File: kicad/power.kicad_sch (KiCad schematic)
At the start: 102 parts

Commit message: Fixed symbol missmatches from upgrading to kicad 6
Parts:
- C? (x16): symbol Device:CP_Small -> Device:C_Polarized_Small
- NT? (x6): symbol Device:Net-Tie_2 -> Device:NetTie_2
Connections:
- net +12V: now also NT?.2
- net +5V: now also NT?.2
- net GND: now also C?.2, C?.2, C?.2, C?.2, C?.2, C?.2, C?.2, C?.2, C?.2, C?.2
- net SVOUT: now also NT?.2
- net VDD: now also C?.1, NT?.1, NT?.1, NT?.1
- net at C?.1, C?.1, U?.2 (VIN)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: now also C?.1, C?.1, NT?.2 (x3)
- net at C?.1, C?.1, C?.2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: now also C?.1, C?.1, NT?.1
- net at Q?.1 (B), R?.1, R?.2: now also C?.1
- net at C?.1, C?.1, C?.1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: now also C?.1, C?.1, NT?.1 (x2)
- new net: C?.2, C?.2 (x3)
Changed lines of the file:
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@@
     (pin "1")
   )
-  (symbol (lib_id "Device:CP_Small") (at 189.865 52.705 0) (unit 1)
+  (symbol (lib_id "Device:C_Polarized_Small") (at 189.865 52.705 0) (unit 1)
     (in_bom yes) (on_board yes)
     (property "Reference" "C?" (id 0) (at 192.1002 51.5366 0)
@@
       (effects (font (size 1.27 1.27)) hide)
     )
+    (pin "1")
+    (pin "2")
   )
   (symbol (lib_id "Diode_Bridge:GBU6M") (at 177.8 50.165 0) (unit 1)
@@
     (pin "4")
   )
-  (symbol (lib_id "power:PWR_FLAG") (at 30.48 25.4 270)
+  (symbol (lib_id "power:PWR_FLAG") (at 30.48 25.4 270) (unit 1)
     (in_bom yes) (on_board yes)
     (property "Reference" "#FLG?" (id 0) (at 32.385 25.4 0)
@@
     (pin "1")
   )
-  (symbol (lib_id "power:PWR_FLAG") (at 30.48 27.94 270)
+  (symbol (lib_id "power:PWR_FLAG") (at 30.48 27.94 270) (unit 1)
     (in_bom yes) (on_board yes)
     (property "Reference" "#FLG?" (id 0) (at 32.385 27.94 0)
@@
     (pin "1")
   )
-  (symbol (lib_id "Device:CP_Small") (at 200.025 52.705 0) (unit 1)
+  (symbol (lib_id "Device:C_Polarized_Small") (at 200.025 52.705 0) (unit 1)
     (in_bom yes) (on_board yes)
     (property "Reference" "C?" (id 0) (at 202.2602 51.5366 0)
@@
       (effects (font (size 1.27 1.27)) hide)
     )
+    (pin "1")
+    (pin "2")
   )
   (symbol (lib_id "power:GND") (at 189.865 55.245 0) (unit 1)
@@
     (pin "2")
   )
-  (symbol (lib_id "Device:CP_Small") (at 232.41 56.515 0) (unit 1)
+  (symbol (lib_id "Device:C_Polarized_Small") (at 232.41 56.515 0) (unit 1)
     (in_bom yes) (on_board yes)
     (property "Reference" "C?" (id 0) (at 226.695 55.88 0)
@@
       (effects (font (size 1.27 1.27)) hide)
     )
+    (pin "1")
+    (pin "2")
   )
   (symbol (lib_id "power:GND") (at 232.41 62.23 0) (unit 1)
@@
     (pin "2")
   )
-  (symbol (lib_id "Device:CP_Small") (at 109.22 117.475 0) (mirror y) (unit 1)
+  (symbol (lib_id "Device:C_Polarized_Small") (at 109.22 117.475 0) (mirror y) (unit 1)
     (in_bom yes) (on_board yes)
     (property "Reference" "C?" (id 0) (at 114.3 116.205 0)
@@
       (effects (font (size 1.27 1.27)) hide)
     )
-  )
-  (symbol (lib_id "Device:CP_Small") (at 109.22 109.22 180) (unit 1)
+    (pin "1")
+    (pin "2")
+  )
+  (symbol (lib_id "Device:C_Polarized_Small") (at 109.22 109.22 180) (unit 1)
     (in_bom yes) (on_board yes)
     (property "Reference" "C?" (id 0) (at 113.665 107.95 0)
@@
       (effects (font (size 1.27 1.27)) hide)
     )
+    (pin "1")
+    (pin "2")
   )
   (symbol (lib_id "Device:C_Small") (at 29.845 111.76 0) (unit 1)
@@
     (pin "2")
   )
-  (symbol (lib_id "Device:CP_Small") (at 29.845 104.14 180) (unit 1)
+  (symbol (lib_id "Device:C_Polarized_Small") (at 29.845 104.14 180) (unit 1)
     (in_bom yes) (on_board yes)
     (property "Reference" "C?" (id 0) (at 34.925 105.41 0)
@@
       (effects (font (size 1.27 1.27)) hide)
     )
-  )
-  (symbol (lib_id "Device:CP_Small") (at 21.59 104.14 180) (unit 1)
+    (pin "1")
+    (pin "2")
+  )
+  (symbol (lib_id "Device:C_Polarized_Small") (at 21.59 104.14 180) (unit 1)
     (in_bom yes) (on_board yes)
     (property "Reference" "C?" (id 0) (at 26.67 105.41 0)
@@
       (effects (font (size 1.27 1.27)) hide)
     )
-  )
-  (symbol (lib_id "power:VDD") (at 15.875 106.045 0)
+    (pin "1")
+    (pin "2")
+  )
+  (symbol (lib_id "power:VDD") (at 15.875 106.045 0) (unit 1)
     (in_bom yes) (on_board yes)
     (property "Reference" "#PWR?" (id 0) (at 15.875 109.855 0)
@@
     (pin "2")
   )
-  (symbol (lib_id "Device:CP_Small") (at 29.21 53.34 180) (unit 1)
+  (symbol (lib_id "Device:C_Polarized_Small") (at 29.21 53.34 180) (unit 1)
     (in_bom yes) (on_board yes)
     (property "Reference" "C?" (id 0) (at 34.29 54.61 0)
@@
       (effects (font (size 1.27 1.27)) hide)
     )
-  )
-  (symbol (lib_id "Device:CP_Small") (at 20.955 53.34 180) (unit 1)
+    (pin "1")
+    (pin "2")
+  )
+  (symbol (lib_id "Device:C_Polarized_Small") (at 20.955 53.34 180) (unit 1)
     (in_bom yes) (on_board yes)
     (property "Reference" "C?" (id 0) (at 26.035 54.61 0)
@@
       (effects (font (size 1.27 1.27)) hide)
     )
-  )
-  (symbol (lib_id "power:VDD") (at 15.24 55.245 0)
+    (pin "1")
+    (pin "2")
+  )
+  (symbol (lib_id "power:VDD") (at 15.24 55.245 0) (unit 1)
     (in_bom yes) (on_board yes)
     (property "Reference" "#PWR?" (id 0) (at 15.24 59.055 0)
@@
     (pin "1")
   )
-  (symbol (lib_id "Device:Net-Tie_2") (at 18.415 57.15 0) (unit 1)
+  (symbol (lib_id "Device:NetTie_2") (at 18.415 57.15 0) (unit 1)
     (in_bom yes) (on_board yes)
     (property "Reference" "NT?" (id 0) (at 18.415 55.88 0))
@@
       (effects (font (size 1.27 1.27)) hide)
     )
-  )
-  (symbol (lib_id "Device:Net-Tie_2") (at 19.05 107.95 0) (unit 1)
+    (pin "1")
+    (pin "2")
+  )
+  (symbol (lib_id "Device:NetTie_2") (at 19.05 107.95 0) (unit 1)
     (in_bom yes) (on_board yes)
     (property "Reference" "NT?" (id 0) (at 19.05 106.68 0))
@@
       (effects (font (size 1.27 1.27)) hide)
     )
+    (pin "1")
+    (pin "2")
   )
   (symbol (lib_id "power:GND") (at 78.105 147.32 0) (unit 1)
@@
     (pin "2")
   )
-  (symbol (lib_id "Device:CP_Small") (at 99.695 66.675 0) (mirror y) (unit 1)
+  (symbol (lib_id "Device:C_Polarized_Small") (at 99.695 66.675 0) (mirror y) (unit 1)
     (in_bom yes) (on_board yes)
     (property "Reference" "C?" (id 0) (at 104.775 65.405 0)
@@
       (effects (font (size 1.27 1.27)) hide)
     )
-  )
-  (symbol (lib_id "Device:CP_Small") (at 99.695 58.42 180) (unit 1)
+    (pin "1")
+    (pin "2")
+  )
+  (symbol (lib_id "Device:C_Polarized_Small") (at 99.695 58.42 180) (unit 1)
     (in_bom yes) (on_board yes)
     (property "Reference" "C?" (id 0) (at 104.14 57.15 0)
@@
       (effects (font (size 1.27 1.27)) hide)
     )
+    (pin "1")
+    (pin "2")
   )
   (symbol (lib_id "power:GND") (at 80.01 69.85 0) (unit 1)
@@
     (pin "2")
   )
-  (symbol (lib_id "Device:Net-Tie_2") (at 106.045 62.23 0) (unit 1)
+  (symbol (lib_id "Device:NetTie_2") (at 106.045 62.23 0) (unit 1)
     (in_bom yes) (on_board yes)
     (property "Reference" "NT?" (id 0) (at 106.045 60.96 0))
@@
       (effects (font (size 1.27 1.27)) hide)
     )
-  )
-  (symbol (lib_id "Device:Net-Tie_2") (at 115.57 113.03 0) (unit 1)
+    (pin "1")
+    (pin "2")
+  )
+  (symbol (lib_id "Device:NetTie_2") (at 115.57 113.03 0) (unit 1)
     (in_bom yes) (on_board yes)
     (property "Reference" "NT?" (id 0) (at 115.57 111.76 0))
@@
       (effects (font (size 1.27 1.27)) hide)
     )
+    (pin "1")
+    (pin "2")
   )
   (symbol (lib_id "Device:R") (at 78.105 142.24 0) (unit 1)
@@
     )
   )
-  (symbol (lib_id "Device:CP_Small") (at 242.57 44.45 0) (unit 1)
+  (symbol (lib_id "Device:C_Polarized_Small") (at 242.57 44.45 0) (unit 1)
     (in_bom yes) (on_board yes)
     (property "Reference" "C?" (id 0) (at 244.8052 43.2816 0)
@@
       (effects (font (size 1.27 1.27)) hide)
     )
+    (pin "1")
+    (pin "2")
   )
   (symbol (lib_id "power:GND") (at 242.57 46.99 0) (unit 1)
@@
     (pin "2")
   )
-  (symbol (lib_id "Device:CP_Small") (at 227.33 117.475 0) (mirror y) (unit 1)
+  (symbol (lib_id "Device:C_Polarized_Small") (at 227.33 117.475 0) (mirror y) (unit 1)
     (in_bom yes) (on_board yes)
     (property "Reference" "C?" (id 0) (at 232.41 116.205 0)
@@
       (effects (font (size 1.27 1.27)) hide)
     )
+    (pin "1")
+    (pin "2")
   )
   (symbol (lib_id "Device:C_Small") (at 147.955 111.76 0) (unit 1)
@@
     (pin "2")
   )
-  (symbol (lib_id "Device:CP_Small") (at 147.955 104.14 180) (unit 1)
+  (symbol (lib_id "Device:C_Polarized_Small") (at 147.955 104.14 180) (unit 1)
     (in_bom yes) (on_board yes)
     (property "Reference" "C?" (id 0) (at 153.035 105.41 0)
@@
       (effects (font (size 1.27 1.27)) hide)
     )
-  )
-  (symbol (lib_id "Device:CP_Small") (at 139.7 104.14 180) (unit 1)
+    (pin "1")
+    (pin "2")
+  )
+  (symbol (lib_id "Device:C_Polarized_Small") (at 139.7 104.14 180) (unit 1)
     (in_bom yes) (on_board yes)
     (property "Reference" "C?" (id 0) (at 144.78 105.41 0)
@@
       (effects (font (size 1.27 1.27)) hide)
     )
-  )
-  (symbol (lib_id "power:VDD") (at 133.985 106.045 0)
+    (pin "1")
+    (pin "2")
+  )
+  (symbol (lib_id "power:VDD") (at 133.985 106.045 0) (unit 1)
     (in_bom yes) (on_board yes)
     (property "Reference" "#PWR?" (id 0) (at 133.985 109.855 0)
@@
     (pin "1")
   )
-  (symbol (lib_id "Device:Net-Tie_2") (at 137.16 107.95 0) (unit 1)
+  (symbol (lib_id "Device:NetTie_2") (at 137.16 107.95 0) (unit 1)
     (in_bom yes) (on_board yes)
     (property "Reference" "NT?" (id 0) (at 137.16 106.68 0))
@@
       (effects (font (size 1.27 1.27)) hide)
     )
+    (pin "1")
+    (pin "2")
   )
   (symbol (lib_id "Device:R") (at 196.215 132.715 0) (unit 1)
@@
     (pin "2")
   )
-  (symbol (lib_id "Device:CP_Small") (at 227.33 109.22 180) (unit 1)
+  (symbol (lib_id "Device:C_Polarized_Small") (at 227.33 109.22 180) (unit 1)
     (in_bom yes) (on_board yes)
     (property "Reference" "C?" (id 0) (at 231.775 107.95 0)
@@
       (effects (font (size 1.27 1.27)) hide)
     )
-  )
-  (symbol (lib_id "Device:Net-Tie_2") (at 233.68 113.03 0) (unit 1)
+    (pin "1")
+    (pin "2")
+  )
+  (symbol (lib_id "Device:NetTie_2") (at 233.68 113.03 0) (unit 1)
     (in_bom yes) (on_board yes)
     (property "Reference" "NT?" (id 0) (at 233.68 111.76 0))
@@
       (effects (font (size 1.27 1.27)) hide)
     )
+    (pin "1")
+    (pin "2")
   )
   (symbol (lib_id "power:+5V") (at 243.84 111.125 0) (unit 1)

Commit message: Fixed broken connections
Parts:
- removed NT? (x6): Net-Tie_2, symbol Device:NetTie_2
- gave numbers to parts that had none: 96
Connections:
- net +12V: now also C24.2, C25.1, L1.2
- net +5V: now also C45.2, C46.1, C48.2, C49.1, C50.2, C51.1, C52.1, C53.1, L3.2
- net GND: now also C12.2, C13.2, C14.2, C15.2, C16.2, C17.2, C18.2, C19.2, C38.2, C39.2, C40.2, C41.2
- net SVOUT: now also C26.2, C27.1, C30.2, C31.1, C34.2, C35.1, L2.2
- net VDD: now also C12.1, C13.1, C14.1, C15.1, C38.1, C39.1, C40.1, C41.1, U3.2 (VIN), U3.3 (EN), U4.2 (VIN), U4.3 (EN), U5.2 (VIN), U5.3 (EN)
- net at D3.1 (+), Q6.2 (C), R52.2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: now also C44.1, C47.1
- new net: C36.1, C37.1
- new net: C18.1, C19.1
- new net: C16.1, C17.1
- new net: C28.2, C29.1
- new net: C32.1, C33.1
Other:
- moved on the sheet: C44, C47, C53, C54, C55, D3, HS3, Q6, R52, R53, R56, R59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

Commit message: Yeeted SMPSs and small changes
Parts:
- removed C12, C14, C16, C18, C32, C33, C36, C37, C38, C40, C52, C53: 47µF, symbol Device:C_Polarized_Small
- removed C13, C15, C28, C29, C30, C31, C34, C35, C39, C48, C49, C50, C51: 1µF, symbol Device:C_Small
- removed C17, C19, C20, C21, C22, C23, C24, C25, C26, C27, C41, C42, C43, C45, C46: 100nF, symbol Device:C_Small
- removed L1: 10µH, symbol Device:L_Small
- removed L2, L3: 40µH, symbol Device:L_Small
- removed Q5: 2N7002K, Package_TO_SOT_SMD:SOT-23, symbol Transistor_FET:2N7002K
- removed R24, R25, R26, R27, R28, R29, R46, R47, R48: 100k, symbol Device:R_Small
- removed R30, R31, R50, R51, R57, R58: 1k, symbol Device:R
- removed R32, R33, R34, R36, R38, R42, R43, R49: 10k, symbol Device:R
- removed R35, R37, R39, R40, R41, R44, R45, R54, R55: 100k, symbol Device:R
- removed TP6: 12V, symbol Connector:TestPoint
- removed TP7: SVOUT, symbol Connector:TestPoint
- removed TP9: 5V, symbol Connector:TestPoint
- removed U3, U4, U5: AP64352, Package_SO:SOIC-8-1EP_3.9x4.9mm_P1.27mm_EP2.41x3.3mm_ThermalVias, symbol symbols:AP64352
- added NT?: NetTie_2, symbol Device:NetTie_2
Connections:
- net VDD: now also NT?.1
- new net VDDA: NT?.2
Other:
- note removed: "12V Regulator @ 1.5A Max"
- note removed: "1MHz/100k"
- note removed: "5V Regulator 2.5A"
- note removed: "Pre regulator 21V/11V @ 2.5A Max"
- moved on the sheet: C44, C47, C54, C55, D3, HS3, Q6, R52, R53, R56, R59, TP8

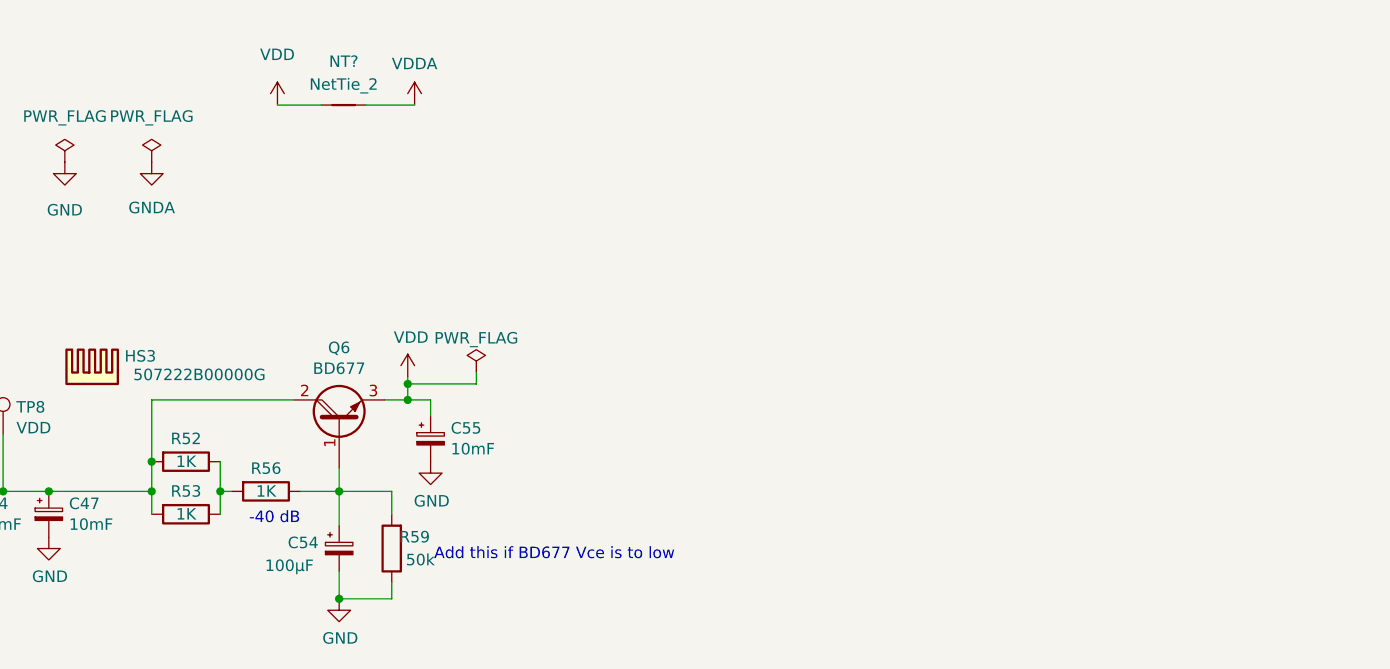
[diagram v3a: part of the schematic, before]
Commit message: Added LM317 for 12V regulation
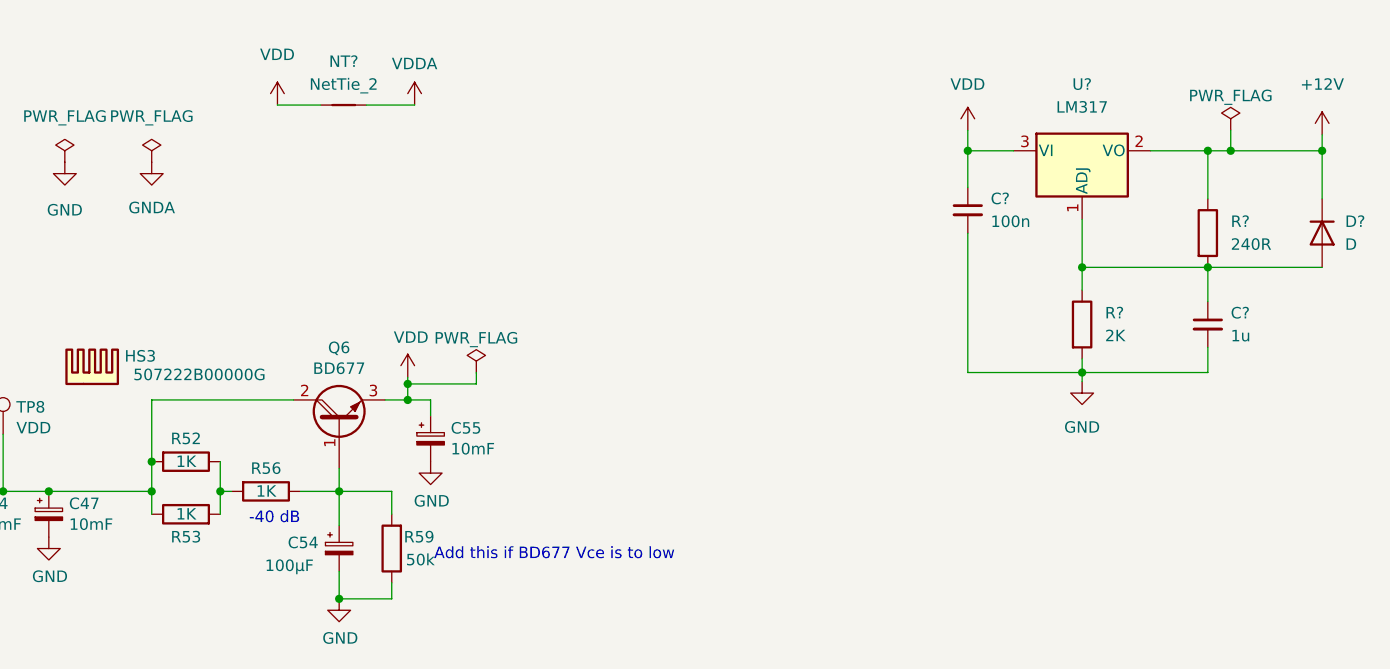
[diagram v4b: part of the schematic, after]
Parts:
- added C?: 100n, symbol Device:C_Small
- added C?: 1u, symbol Device:C_Small
- added D?: D, symbol Device:D
- added R?: 2K, symbol Device:R
- added R?: 240R, symbol Device:R
- added U?: LM317, Package_TO_SOT_THT:TO-220-3_Vertical, symbol Regulator_Linear:LM317_TO-220
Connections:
- net GND: now also C?.2, C?.2, R?.2
- net VDD: now also C?.1, U?.3 (VI)
- net at C44.1, C47.1, D3.1 (+)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: now also R53.1; no longer R53.2
- net at R52.1, R56.2: now also R53.2; no longer R53.1
- new net: C?.1, D?.2 (A), R?.1, R?.2, U?.1 (ADJ)
- new net +12V: D?.1 (K), R?.1, U?.2 (VO)
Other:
- moved on the sheet: R53

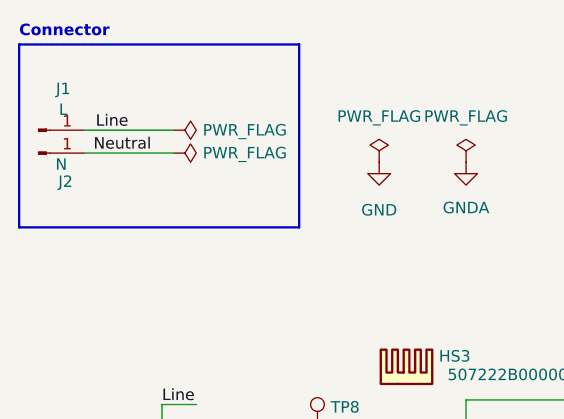
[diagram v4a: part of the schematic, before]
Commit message: Updated files to kicad 8
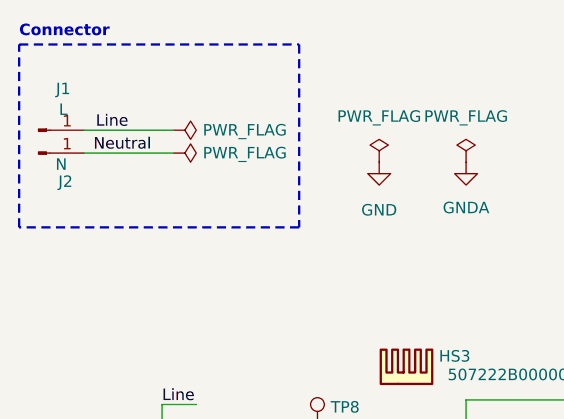
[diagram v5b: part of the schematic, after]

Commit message: Fixed a bunch of alignment
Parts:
- D5: renamed from D3; footprint Diode_THT:Diode_Bridge_Vishay_KBPM -> Diode_THT:Diode_Bridge_Vishay_GBU
- J1, J2: symbol Connector:Conn_01x01_Male -> Connector_Generic:Conn_01x01
- gave numbers to parts that had none: 7
- renumbered C44 to C12, C47 to C13, C54 to C14, C55 to C15, Q6 to Q5, R52 to R24, R53 to R25, R56 to R26, R59 to R27, TP8 to TP6
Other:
- moved on the sheet: C13, C14, C15, D5, J1, J2, NT1, Q5, R25, R26, R27, TP6
